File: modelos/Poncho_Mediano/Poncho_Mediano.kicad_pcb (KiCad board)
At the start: 2 copper layers, 86.4 x 96.5 mm, 7 parts, among them P1 CONN_5, P2 CONN_4

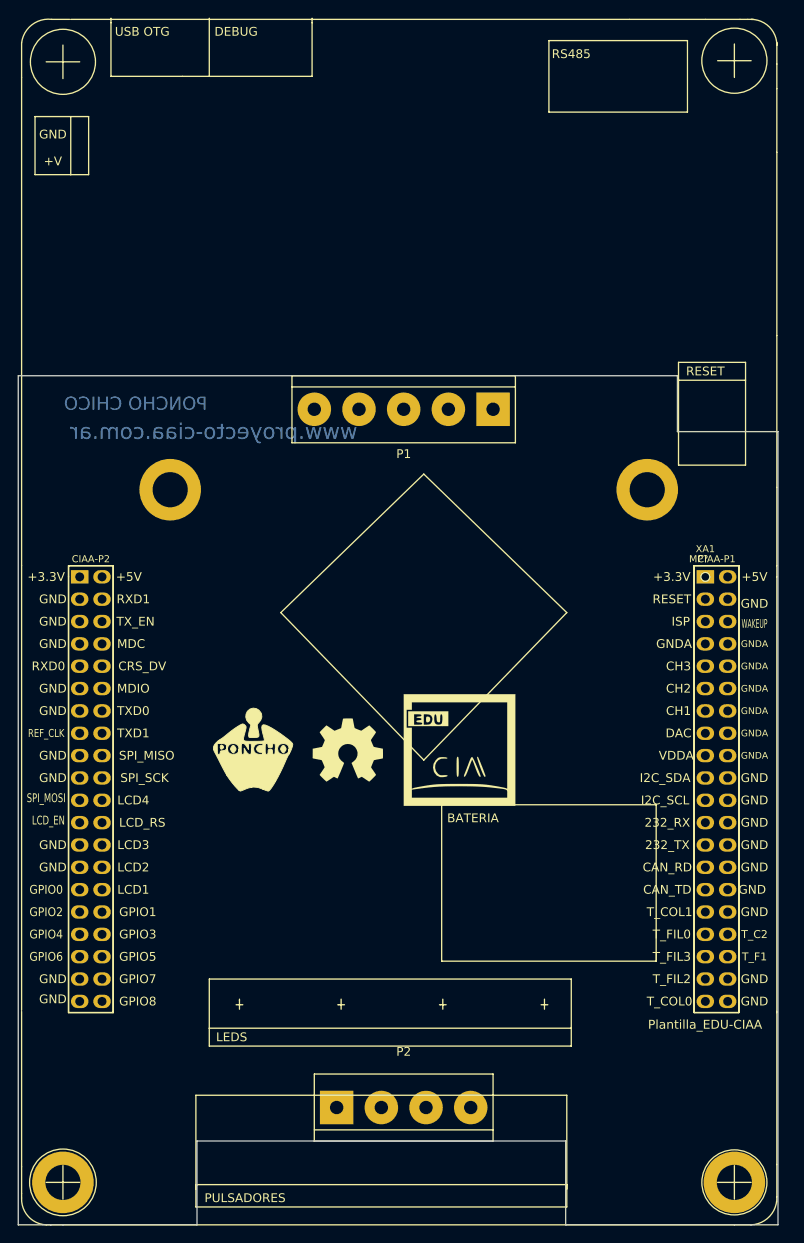
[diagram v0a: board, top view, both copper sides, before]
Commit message: * Agrego ruteo al poncho mediano. Muevo ícono de Template.
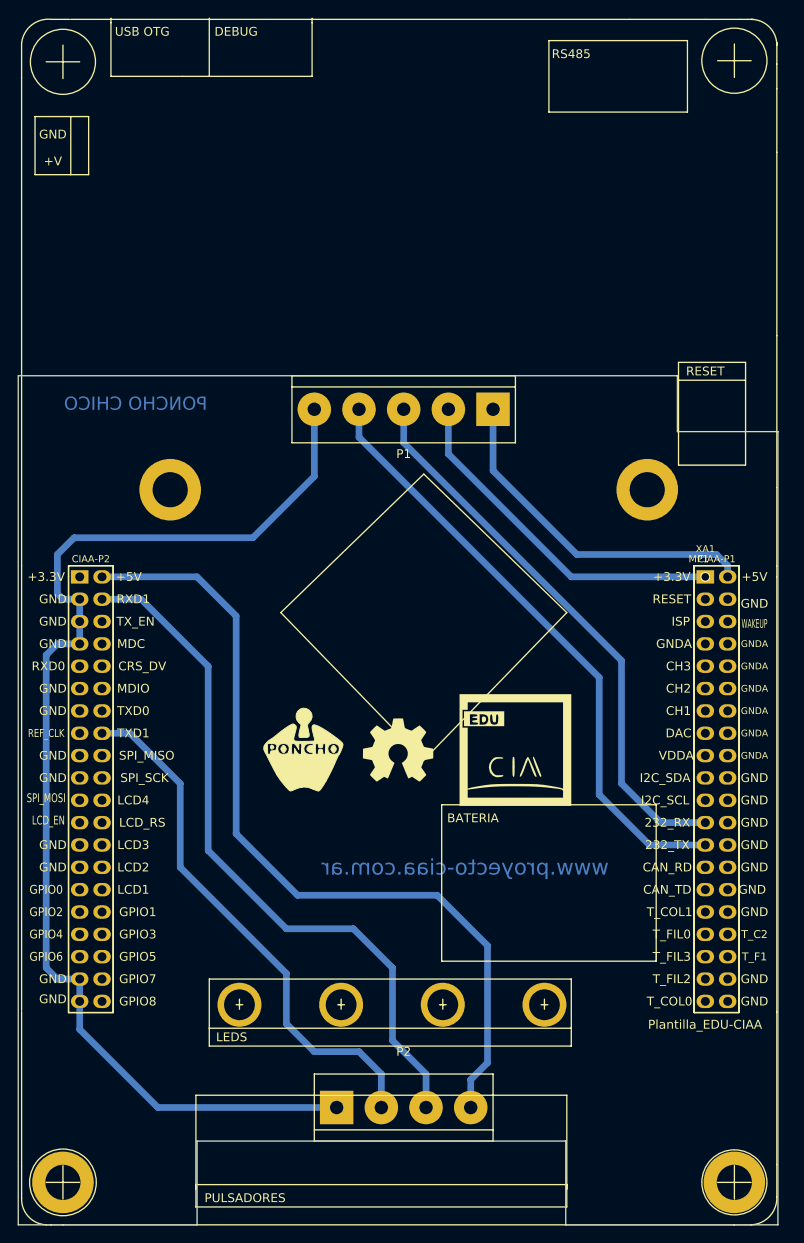
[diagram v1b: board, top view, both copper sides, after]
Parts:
- added H1: PCB_HOLE, Poncho_Modelos:Led_Hole, F.Cu at (89.3, 129.9)
- added H2: PCB_HOLE, Poncho_Modelos:Led_Hole, F.Cu at (100.8, 129.9)
- added H3: PCB_HOLE, Poncho_Modelos:Led_Hole, F.Cu at (112.4, 129.9)
- added H4: PCB_HOLE, Poncho_Modelos:Led_Hole, F.Cu at (124.0, 129.9)
- moved G*** 6.35 mm to (120.7, 101.0)
- moved G101 5.72 mm to (107.3, 101.0)
- moved G*** 5.71 mm to (96.5, 101.0)
- gave numbers to parts that had none: 1
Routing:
- net GND: track 0.00 -> 135.7 mm
- net +5VP: track 0.00 -> 94.9 mm
- net Net-(P2-Pad3): track 0.00 -> 80.1 mm
- net Net-(P1-Pad4): track 0.00 -> 69.6 mm
- net Net-(P1-Pad3): track 0.00 -> 64.2 mm
- net Net-(P2-Pad2): track 0.00 -> 60.5 mm
- net +3.3V: track 0.00 -> 40.1 mm
- net +5V: track 0.00 -> 39.4 mm
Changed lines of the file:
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@@
-(kicad_pcb (version 4) (host pcbnew "(2015-05-19 BZR 5670)-product")
+(kicad_pcb (version 4) (host pcbnew "(2015-08-26 BZR 6128)-product")
   (general
     (links 13)
-    (no_connects 13)
+    (no_connects 0)
     (area 64.059999 58.344999 150.570001 155.015001)
     (thickness 1.6)
     (drawings 42)
-    (tracks 0)
+    (tracks 63)
     (zones 0)
-    (modules 7)
+    (modules 11)
     (nets 9)
   )
@@
   )
   (setup
-    (last_trace_width 0.381)
+    (last_trace_width 0.762)
     (user_trace_width 0.508)
     (user_trace_width 0.635)
@@
   )
   (module Poncho_Esqueleto:Logo_EDU-CIAA (layer F.Cu)
-    (at 114.3 100.965)
+    (at 120.65 100.965)
     (fp_text reference G*** (at 0 7.112) (layer F.SilkS) hide
       (effects (font (thickness 0.3048)))
@@
   )
   (module Poncho_Esqueleto:Logo_Poncho (layer F.Cu)
-    (at 90.805 100.965)
+    (at 96.52 100.965)
     (fp_text reference G*** (at 0.127 5.588) (layer F.SilkS) hide
       (effects (font (thickness 0.3)))
@@
   )
   (module Poncho_Esqueleto:Logo_OSHWA (layer F.Cu)
-    (at 101.6 100.965)
+    (at 107.315 100.965)
     (fp_text reference G101 (at 0 4.2418) (layer F.SilkS) hide
       (effects (font (size 0.7112 0.4572) (thickness 0.1143)))
@@
     (at 142.24 81.28)
     (tags "plantilla poncho EDU CIAA")
-    (fp_text reference MP? (at -0.762 -2.032) (layer F.SilkS)
+    (fp_text reference MP1 (at -0.762 -2.032) (layer F.SilkS)
       (effects (font (size 0.8 0.8) (thickness 0.12)))
     )
@@
     (fp_line (start 3.81 -1.27) (end -1.27 -1.27) (layer F.SilkS) (width 0.15))
   )
+  (module Poncho_Modelos:Led_Hole (layer F.Cu)
+    (at 89.281 129.921)
+    (fp_text reference H1 (at 0.127 3.937) (layer F.SilkS) hide
+      (effects (font (size 1 1) (thickness 0.15)))
+    )
+    (fp_text value PCB_HOLE (at 0.127 -3.429) (layer Dwgs.User) hide
+      (effects (font (size 1 1) (thickness 0.15)))
+    )
+    (pad 1 thru_hole circle (at 0 0) (size 5 5) (drill 3.5) (layers *.Cu *.Mask F.SilkS))
+  )
+  (module Poncho_Modelos:Led_Hole (layer F.Cu)
+    (at 100.838 129.921)
+    (fp_text reference H2 (at 0.127 3.937) (layer F.SilkS) hide
+      (effects (font (size 1 1) (thickness 0.15)))
+    )
+    (fp_text value PCB_HOLE (at 0.127 -3.429) (layer Dwgs.User) hide
+      (effects (font (size 1 1) (thickness 0.15)))
+    )
+    (pad 1 thru_hole circle (at 0 0) (size 5 5) (drill 3.5) (layers *.Cu *.Mask F.SilkS))
+  )
+  (module Poncho_Modelos:Led_Hole (layer F.Cu)
+    (at 112.395 129.921)
+    (fp_text reference H3 (at 0.127 3.937) (layer F.SilkS) hide
+      (effects (font (size 1 1) (thickness 0.15)))
+    )
+    (fp_text value PCB_HOLE (at 0.127 -3.429) (layer Dwgs.User) hide
+      (effects (font (size 1 1) (thickness 0.15)))
+    )
+    (pad 1 thru_hole circle (at 0 0) (size 5 5) (drill 3.5) (layers *.Cu *.Mask F.SilkS))
+  )
+  (module Poncho_Modelos:Led_Hole (layer F.Cu)
+    (at 123.952 129.921)
+    (fp_text reference H4 (at 0.127 3.937) (layer F.SilkS) hide
+      (effects (font (size 1 1) (thickness 0.15)))
+    )
+    (fp_text value PCB_HOLE (at 0.127 -3.429) (layer Dwgs.User) hide
+      (effects (font (size 1 1) (thickness 0.15)))
+    )
+    (pad 1 thru_hole circle (at 0 0) (size 5 5) (drill 3.5) (layers *.Cu *.Mask F.SilkS))
+  )
   (dimension 86.36 (width 0.3) (layer Dwgs.User)
     (gr_text 86,360mm (at 107.315 161.37) (layer Dwgs.User)
@@
     (effects (font (size 1.5 1.5) (thickness 0.3)) (justify left))
   )
-  (gr_text www.proyecto-ciaa.com.ar (at 86.36 64.77) (layer B.Cu)
+  (gr_text www.proyecto-ciaa.com.ar (at 114.935 114.3) (layer B.Cu)
     (effects (font (size 1.778 1.778) (thickness 0.254)) (justify mirror))
   )
@@
     (effects (font (size 1.5 1.5) (thickness 0.3)))
   )
+  (segment (start 142.24 81.28) (end 127 81.28) (width 0.762) (layer B.Cu) (net 1))
+  (segment (start 113.03 67.31) (end 113.03 62.23) (width 0.762) (layer B.Cu) (net 1))
+  (segment (start 127 81.28) (end 113.03 67.31) (width 0.762) (layer B.Cu) (net 1))
+  (segment (start 142.24 109.22) (end 137.16 109.22) (width 0.762) (layer B.Cu) (net 2))
+  (segment (start 107.95 66.04) (end 107.95 62.23) (width 0.762) (layer B.Cu) (net 2))
+  (segment (start 132.715 90.805) (end 107.95 66.04) (width 0.762) (layer B.Cu) (net 2))
+  (segment (start 132.715 104.775) (end 132.715 90.805) (width 0.762) (layer B.Cu) (net 2))
+  (segment (start 137.16 109.22) (end 132.715 104.775) (width 0.762) (layer B.Cu) (net 2))
+  (segment (start 144.78 81.28) (end 144.78 80.01) (width 0.762) (layer B.Cu) (net 3))
+  (segment (start 118.11 69.215) (end 118.11 62.23) (width 0.762) (layer B.Cu) (net 3))
+  (segment (start 127.635 78.74) (end 118.11 69.215) (width 0.762) (layer B.Cu) (net 3))
+  (segment (start 143.51 78.74) (end 127.635 78.74) (width 0.762) (layer B.Cu) (net 3))
+  (segment (start 144.78 80.01) (end 143.51 78.74) (width 0.762) (layer B.Cu) (net 3))
+  (segment (start 142.24 111.76) (end 135.89 111.76) (width 0.762) (layer B.Cu) (net 4))
+  (segment (start 102.87 65.405) (end 102.87 62.23) (width 0.762) (layer B.Cu) (net 4))
+  (segment (start 130.175 92.71) (end 102.87 65.405) (width 0.762) (layer B.Cu) (net 4))
+  (segment (start 130.175 106.045) (end 130.175 92.71) (width 0.762) (layer B.Cu) (net 4))
+  (segment (start 135.89 111.76) (end 130.175 106.045) (width 0.762) (layer B.Cu) (net 4))
+  (segment (start 71.12 86.36) (end 71.12 83.82) (width 0.762) (layer B.Cu) (net 5))
+  (segment (start 71.12 88.9) (end 71.12 86.36) (width 0.762) (layer B.Cu) (net 5))
+  (segment (start 71.12 127) (end 68.58 127) (width 0.762) (layer B.Cu) (net 5))
+  (segment (start 68.58 88.9) (end 71.12 88.9) (width 0.762) (layer B.Cu) (net 5))
+  (segment (start 67.31 90.17) (end 68.58 88.9) (width 0.762) (layer B.Cu) (net 5))
+  (segment (start 67.31 125.73) (end 67.31 90.17) (width 0.762) (layer B.Cu) (net 5))
+  (segment (start 68.58 127) (end 67.31 125.73) (width 0.762) (layer B.Cu) (net 5))
+  (segment (start 71.12 129.54) (end 71.12 127) (width 0.762) (layer B.Cu) (net 5))
+  (segment (start 71.12 83.82) (end 69.215 83.82) (width 0.762) (layer B.Cu) (net 5))
+  (segment (start 69.215 83.82) (end 68.58 83.185) (width 0.762) (layer B.Cu) (net 5))
+  (segment (start 68.58 83.185) (end 68.58 78.74) (width 0.762) (layer B.Cu) (net 5))
+  (segment (start 68.58 78.74) (end 70.485 76.835) (width 0.762) (layer B.Cu) (net 5))
+  (segment (start 70.485 76.835) (end 90.805 76.835) (width 0.762) (layer B.Cu) (net 5))
+  (segment (start 90.805 76.835) (end 97.79 69.85) (width 0.762) (layer B.Cu) (net 5))
+  (segment (start 97.79 69.85) (end 97.79 62.23) (width 0.762) (layer B.Cu) (net 5))
+  (segment (start 100.33 141.605) (end 80.01 141.605) (width 0.762) (layer B.Cu) (net 5))
+  (segment (start 71.12 132.715) (end 71.12 129.54) (width 0.762) (layer B.Cu) (net 5))
+  (segment (start 80.01 141.605) (end 71.12 132.715) (width 0.762) (layer B.Cu) (net 5))
+  (segment (start 105.41 141.605) (end 105.41 137.795) (width 0.762) (layer B.Cu) (net 6))
+  (segment (start 76.835 99.06) (end 73.66 99.06) (width 0.762) (layer B.Cu) (net 6))
+  (segment (start 82.55 104.775) (end 76.835 99.06) (width 0.762) (layer B.Cu) (net 6))
+  (segment (start 82.55 114.3) (end 82.55 104.775) (width 0.762) (layer B.Cu) (net 6))
+  (segment (start 94.615 126.365) (end 82.55 114.3) (width 0.762) (layer B.Cu) (net 6))
+  (segment (start 94.615 132.08) (end 94.615 126.365) (width 0.762) (layer B.Cu) (net 6))
+  (segment (start 97.79 135.255) (end 94.615 132.08) (width 0.762) (layer B.Cu) (net 6))
+  (segment (start 102.87 135.255) (end 97.79 135.255) (width 0.762) (layer B.Cu) (net 6))
+  (segment (start 105.41 137.795) (end 102.87 135.255) (width 0.762) (layer B.Cu) (net 6))
+  (segment (start 110.49 141.605) (end 110.49 137.795) (width 0.762) (layer B.Cu) (net 7))
+  (segment (start 78.105 83.82) (end 73.66 83.82) (width 0.762) (layer B.Cu) (net 7))
+  (segment (start 85.725 91.44) (end 78.105 83.82) (width 0.762) (layer B.Cu) (net 7))
+  (segment (start 85.725 112.395) (end 85.725 91.44) (width 0.762) (layer B.Cu) (net 7))
+  (segment (start 94.615 121.285) (end 85.725 112.395) (width 0.762) (layer B.Cu) (net 7))
+  (segment (start 102.235 121.285) (end 94.615 121.285) (width 0.762) (layer B.Cu) (net 7))
+  (segment (start 106.68 125.73) (end 102.235 121.285) (width 0.762) (layer B.Cu) (net 7))
+  (segment (start 106.68 133.985) (end 106.68 125.73) (width 0.762) (layer B.Cu) (net 7))
+  (segment (start 110.49 137.795) (end 106.68 133.985) (width 0.762) (layer B.Cu) (net 7))
+  (segment (start 115.57 141.605) (end 115.57 138.43) (width 0.762) (layer B.Cu) (net 8))
+  (segment (start 84.455 81.28) (end 73.66 81.28) (width 0.762) (layer B.Cu) (net 8))
+  (segment (start 88.9 85.725) (end 84.455 81.28) (width 0.762) (layer B.Cu) (net 8))
+  (segment (start 88.9 110.49) (end 88.9 85.725) (width 0.762) (layer B.Cu) (net 8))
+  (segment (start 95.885 117.475) (end 88.9 110.49) (width 0.762) (layer B.Cu) (net 8))
+  (segment (start 111.76 117.475) (end 95.885 117.475) (width 0.762) (layer B.Cu) (net 8))
+  (segment (start 117.475 123.19) (end 111.76 117.475) (width 0.762) (layer B.Cu) (net 8))
+  (segment (start 117.475 136.525) (end 117.475 123.19) (width 0.762) (layer B.Cu) (net 8))
+  (segment (start 115.57 138.43) (end 117.475 136.525) (width 0.762) (layer B.Cu) (net 8))
 )
